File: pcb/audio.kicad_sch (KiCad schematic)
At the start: 0 parts

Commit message: WIP schematic
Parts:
- added C10, C8, C9: 0.1µF, symbol Device:C_Small
- added C5, C6, C7: 0.33µF, symbol Device:C_Small
- added D1, D2, D3: RED, symbol Device:LED_Small_Filled
- added HS1: OMNI-220-18-75-3C, symbol Mechanical:Heatsink_Pad_2Pin
- added Q1, Q2, Q3: BC547, Package_TO_SOT_THT:TO-92_Inline, symbol Transistor_BJT:BC547
- added R1, R3: 910Ω, symbol Device:R_Small
- added R10, R11, R12, R13, R14, R15, R16, R4, R5, R6, R7, R8, R9: R, symbol Device:R
- added R2: 390Ω, symbol Device:R_Small
- added TP1, TP2, TP3, TP4, TP5, TP6, TP7: TestPoint_Probe, symbol Connector:TestPoint_Probe
- added U52: LM7809_TO220, Package_TO_SOT_THT:TO-220-3_Vertical, symbol Regulator_Linear:LM7809_TO220
- added U53: LM7805_TO220, Package_TO_SOT_THT:TO-220-3_Vertical, symbol Regulator_Linear:LM7805_TO220
- added U54: LM7909_TO220, Package_TO_SOT_THT:TO-220-3_Vertical, symbol Regulator_Linear:LM7909_TO220
- added U55, U58: 4504, symbol 4xxx:4504
- added U56, U57, U59, U61: 4053, symbol 4xxx:4053
- added U60: TL072, symbol Amplifier_Operational:TL072
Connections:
- new net: R11.1, U61.14 (X)
- new net: R11.2, R12.2, R13.2, R14.2, R15.2, R16.1, U60.6 (-)
- new net: Q3.2 (B), R6.2
- new net: D2.2 (A), R2.2
- new net: Q2.2 (B), R5.2
- new net: Q1.2 (B), R4.2
- new net: D1.2 (A), R1.2
- new net: U58.12 (Eout), U59.10 (B)
- new net: U58.10 (Dout), U59.11 (A)
- new net: U59.12 (X0), U61.12 (X0)
- new net: R7.1, U59.14 (X)
- new net: R8.1, U59.15 (Y)
- new net: U59.2 (Y0), U61.2 (Y0)
- new net: R9.1, U59.4 (Z)
- new net: U57.2 (Y0), U59.5 (Z0), U61.5 (Z0)
- new net: U58.15 (Fout), U59.9 (C)
- new net: R10.1, R7.2, R8.2, R9.2, U60.2 (-)
- new net: U55.10 (Dout), U57.11 (A)
- new net: U55.12 (Eout), U57.10 (B)
- new net: U55.15 (Fout), U57.9 (C)
- new net: U55.2 (Aout), U56.11 (A)
- new net: U55.4 (Bout), U56.10 (B)
- new net: U55.6 (Cout), U56.9 (C)
- new net: U58.4 (Bout), U61.10 (B)
- new net: U58.2 (Aout), U61.11 (A)
- new net: R12.1, U61.15 (Y)
- new net: R13.1, U61.4 (Z)
- new net: U58.6 (Cout), U61.9 (C)
- new net: D3.1 (K), R3.2
- new net: R10.2, U60.1
- new net: R16.2, U60.7
- new net: U57.14 (X), U57.5 (Z0)
- new net +12V: C5.1, C6.1, TP1.1, TP2.1, U52.1 (VI), U53.1 (VI)
- new net +5VA: C9.1, R2.1, TP6.1, U53.3 (VO), U55.1 (VCC), U58.1 (VCC)
- new net +9VA: C8.1, R1.1, TP5.1, U52.3 (VO), U55.16 (VDD), U56.16 (VDD), U57.16 (VDD), U58.16 (VDD), U59.16 (VDD), U60.8 (V+), U61.16 (VDD)
- new net -12V: C7.1, TP3.1, U54.2 (VI)
- new net -9VA: C10.1, R3.1, TP7.1, U54.3 (VO), U56.7 (VEE), U57.7 (VEE), U59.7 (VEE), U60.4 (V-), U61.7 (VEE)
- new net DC3: U55.14 (Fin)
- new net FILTER0: U58.9 (Din)
- new net FILTER1: U58.11 (Ein)
- new net FILTER2: U58.14 (Fin)
- new net FM12: U55.11 (Ein)
- new net GNDA: C10.2, C5.2, C6.2, C7.2, C8.2, C9.2, D1.1 (K), D2.1 (K), D3.2 (A), HS1.1, HS1.2, Q1.3 (E), Q2.3 (E), Q3.3 (E), TP4.1, U52.2 (GND), U53.2 (GND), U54.1 (GND), U55.8 (VSS), U56.6 (Inh), U56.8 (VSS), U57.6 (Inh), U57.8 (VSS), U58.8 (VSS), U59.1 (Y1), U59.13 (X1), U59.3 (Z1), U59.6 (Inh), U59.8 (VSS), U60.3 (+), U60.5 (+), U61.1 (Y1), U61.13 (X1), U61.3 (Z1), U61.6 (Inh), U61.8 (VSS)
- new net MIX0: U58.3 (Ain)
- new net MIX1: U58.5 (Bin)
- new net MIX2: U58.7 (Cin)
- new net OCTAVE0: R4.1
- new net OCTAVE2: R5.1
- new net OCTAVE3: R6.1
- new net Voice 0/FM/OCTAVE: Q1.1 (C)
- new net Voice 0/SQUARE: U56.12 (X0)
- new net Voice 0/TRIANGLE: U56.13 (X1)
- new net Voice 1/FM/OCTAVE: U57.1 (Y1)
- new net Voice 1/SQUARE: U56.2 (Y0)
- new net Voice 1/TRIANGLE: U56.1 (Y1)
- new net Voice 2/FM/OCTAVE: Q2.1 (C)
- new net Voice 2/SQUARE: U56.5 (Z0)
- new net Voice 2/TRIANGLE: U56.3 (Z1)
- new net Voice 3/FM/OCTAVE: Q3.1 (C)
- new net Voice 3/SQUARE: U57.12 (X0)
- new net Voice 3/TRIANGLE: U57.13 (X1)
- new net WAVEFORM0: U55.3 (Ain)
- new net WAVEFORM1: U55.5 (Bin)
- new net WAVEFORM2: U55.7 (Cin)
- new net WAVEFORM3: U55.9 (Din)
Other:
- added sheet Filter (filter.kicad_sch)
- added sheet Volume 0 (volume.kicad_sch)
- added sheet Volume 1 (volume.kicad_sch)
- added sheet Volume 2 (volume.kicad_sch)
- added sheet Volume 3 (volume.kicad_sch)
- sheet Voice 0 ports: added FM/OCTAVE, PWM, SQUARE, TRIANGLE; removed none
- sheet Voice 1 ports: added FM/OCTAVE, PWM, SQUARE, TRIANGLE; removed none
- sheet Voice 2 ports: added FM/OCTAVE, PWM, SQUARE, TRIANGLE; removed none
- sheet Voice 3 ports: added FM/OCTAVE, PWM, SQUARE, TRIANGLE; removed none
- note added: "+5VA OK"
- note added: "+9VA OK"
- note added: "-9VA OK"
- note added: "Analog Power"

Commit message: WIP PCB
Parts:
- added Q?: BC547, Package_TO_SOT_THT:TO-92_Inline, symbol Transistor_BJT:BC547
- added R? (x2): 10kΩ, symbol Device:R
- added R?: R, symbol Device:R
- renumbered C9 to C?, C5 to C?, C7 to C?, C10 to C?, C6 to C?, C8 to C?, D2 to D?, D1 to D?, D3 to D?, HS1 to HS?, Q3 to Q?, Q1 to Q?, Q2 to Q?, R11 to R?, R5 to R?, R7 to R?, R4 to R?, R15 to R?, R9 to R?, R8 to R?, R12 to R?, R14 to R?, R16 to R?, R13 to R?, R2 to R?, R10 to R?, R1 to R?, R6 to R?, R3 to R?, TP3 to TP?, TP7 to TP?, TP6 to TP?, TP1 to TP?, TP4 to TP?, TP5 to TP?, TP2 to TP?, U52 to U?, U54 to U?, U59 to U?, U55 to U?, U60 to U?, U53 to U?, U61 to U?, U58 to U?, U56 to U?, U57 to U?
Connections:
- net -9VA: now also R?.2
- net GNDA: now also Q?.3 (E), R?.1
- net Voice 1/FM/OCTAVE: now also U?.15 (Y); no longer U?.1 (Y1)
- net Envelope/OUT0: now reaches U?.12 (X0), U?.12 (X0)
- net Envelope/OUT1: now reaches U?.2 (Y0), U?.2 (Y0)
- net Envelope/OUT2: now reaches U?.2 (Y0), U?.5 (Z0), U?.5 (Z0)
- net Envelope/OUT3: now reaches R?.1
- net Envelope/IN0: now reaches U?.14 (X)
- net Envelope/IN1: now reaches U?.15 (Y)
- net Envelope/IN2: now reaches U?.4 (Z)
- net at U?.3 (Z1): now also R?.1, R?.2
- net Envelope/IN3: now reaches U?.4 (Z)
- new net: Q?.2 (B), R?.2
- new net: Q?.1 (C), U?.1 (Y1)
- new net OCTAVE1: R?.1
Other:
- sheet Volume 0 renamed Envelope
- removed sheet Volume 1
- removed sheet Volume 2
- removed sheet Volume 3
- sheet Envelope ports: added D0, D1, D2, D3, D4, D5, D6, D7, IN0, IN1, IN2, IN3, LOAD0, LOAD1, LOAD2, LOAD3, OUT0, OUT1, OUT2, OUT3; removed none
- moved on the sheet: Q?, R?, U?, U?A, U?B

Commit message: WIP PCB
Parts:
- added R? (x2): 220kΩ, symbol Device:R
- added U? (x7): 74HC14, symbol 74xx:74HC14
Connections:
- net +5VA: now also U?.14 (VCC)
- net GNDA: now also U?.7 (GND)
- net PWM0: now also U?.1
- net PWM1: now also U?.3
- net PWM2: now also U?.5
- net PWM3: now also U?.9
- net Filter/OUT: now reaches R?.1
- net Filter/IN: now reaches R?.2, U?.1
- net at R?.2, U?.7: now also R?.1
- new net: R?.2, U?.12
- new net: R?.2, U?.13
- new net Filter/PWM: U?.10
- new net Filter/Z0: U?.11
- new net Filter/Z1: R?.1
- new net Voice 0/PWM: U?.2
- new net Voice 1/PWM: U?.4
- new net Voice 2/PWM: U?.6
- new net Voice 3/PWM: U?.8
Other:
- sheet Filter ports: added IN, OUT, PWM, RESON0, RESON1, SELECT, Z, Z0, Z1; removed none
- moved on the sheet: Q?, R?, U?, U?A, U?B

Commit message: wip schematic
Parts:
- removed U? (x7): 74HC14, symbol 74xx:74HC14
- added D? (x2): BAT46, Diode_THT:D_DO-35_SOD27_P7.62mm_Horizontal, symbol Diode:BAT46
- added U?: 74HC245, symbol 74xx:74HC245
- R?: value 220kΩ -> 470Ω
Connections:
- net +5VA: now also D?.1 (K), U?.1 (A->B), U?.20 (VCC)
- net GNDA: now also D?.2 (A), U?.10 (GND), U?.8 (A6), U?.9 (A7)
- net PWM0: now also U?.2 (A0)
- net PWM1: now also U?.3 (A1)
- net PWM2: now also U?.4 (A2)
- net PWM3: now also U?.5 (A3)
- net Voice 0/PWM: now also U?.18 (B0)
- net Voice 1/PWM: now also U?.17 (B1)
- net Voice 2/PWM: now also U?.16 (B2)
- net Voice 3/PWM: now also U?.15 (B3)
- net STB5: now reaches R?.2
- net STB5: now also U?.13 (B5)
- net STA5: now reaches R?.2
- net STA5: now also D?.1 (K), D?.2 (A), U?.7 (A5)
- new net FLOAT: U?.19 (CE)
- new net STA4: U?.6 (A4)
- new net STB4: U?.14 (B4)
- no-connect marks 0 -> 2
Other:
- note added: "IN"
- note added: "OUT"

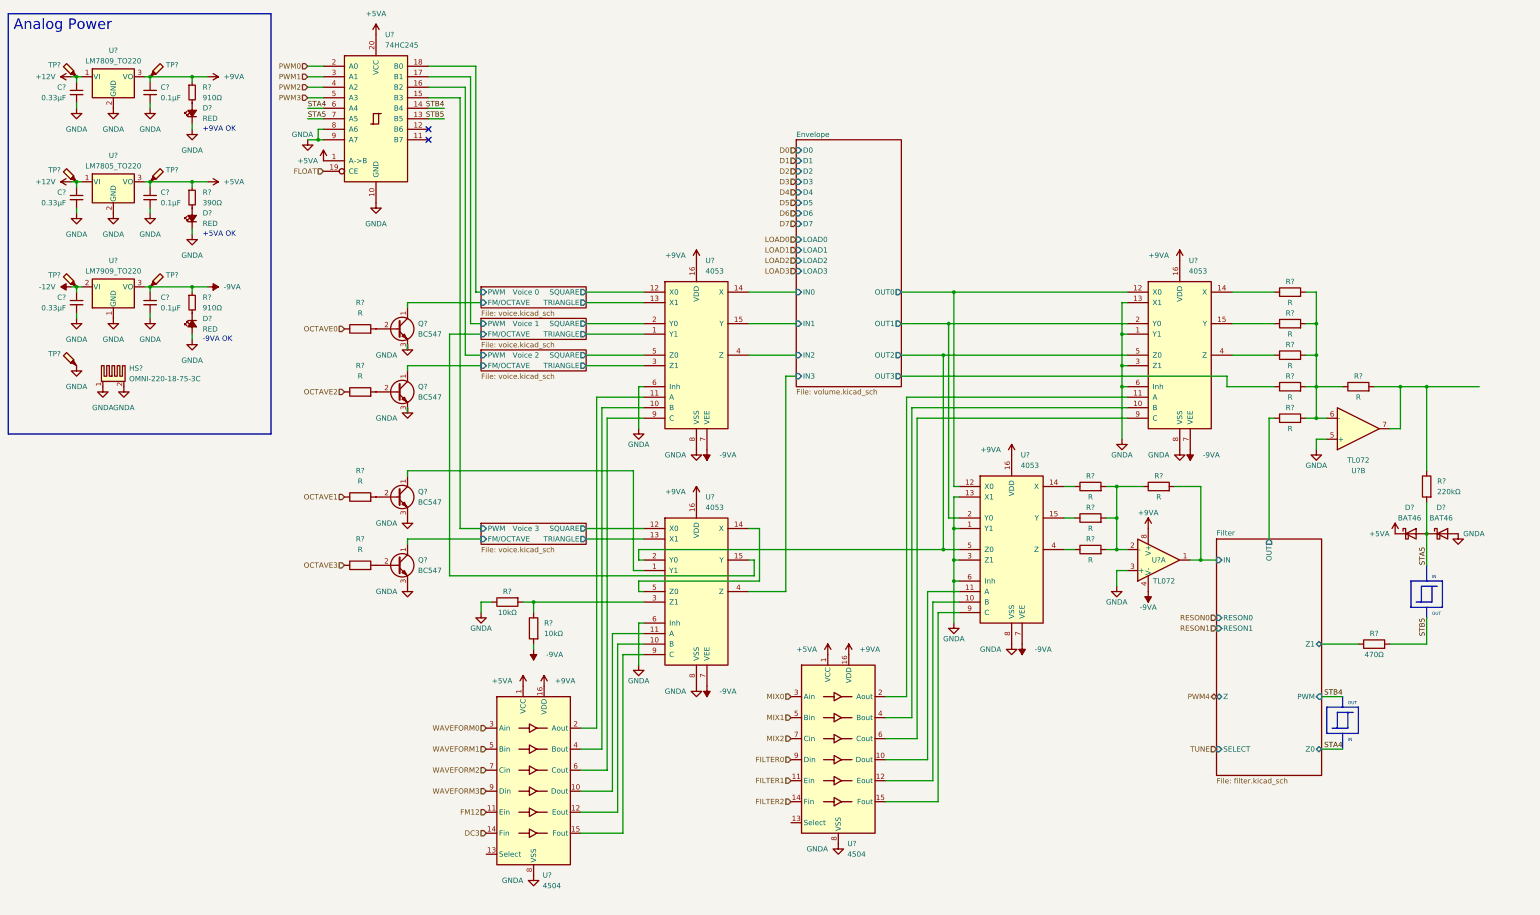
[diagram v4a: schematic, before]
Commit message: PCB: add reset circuit, xtal
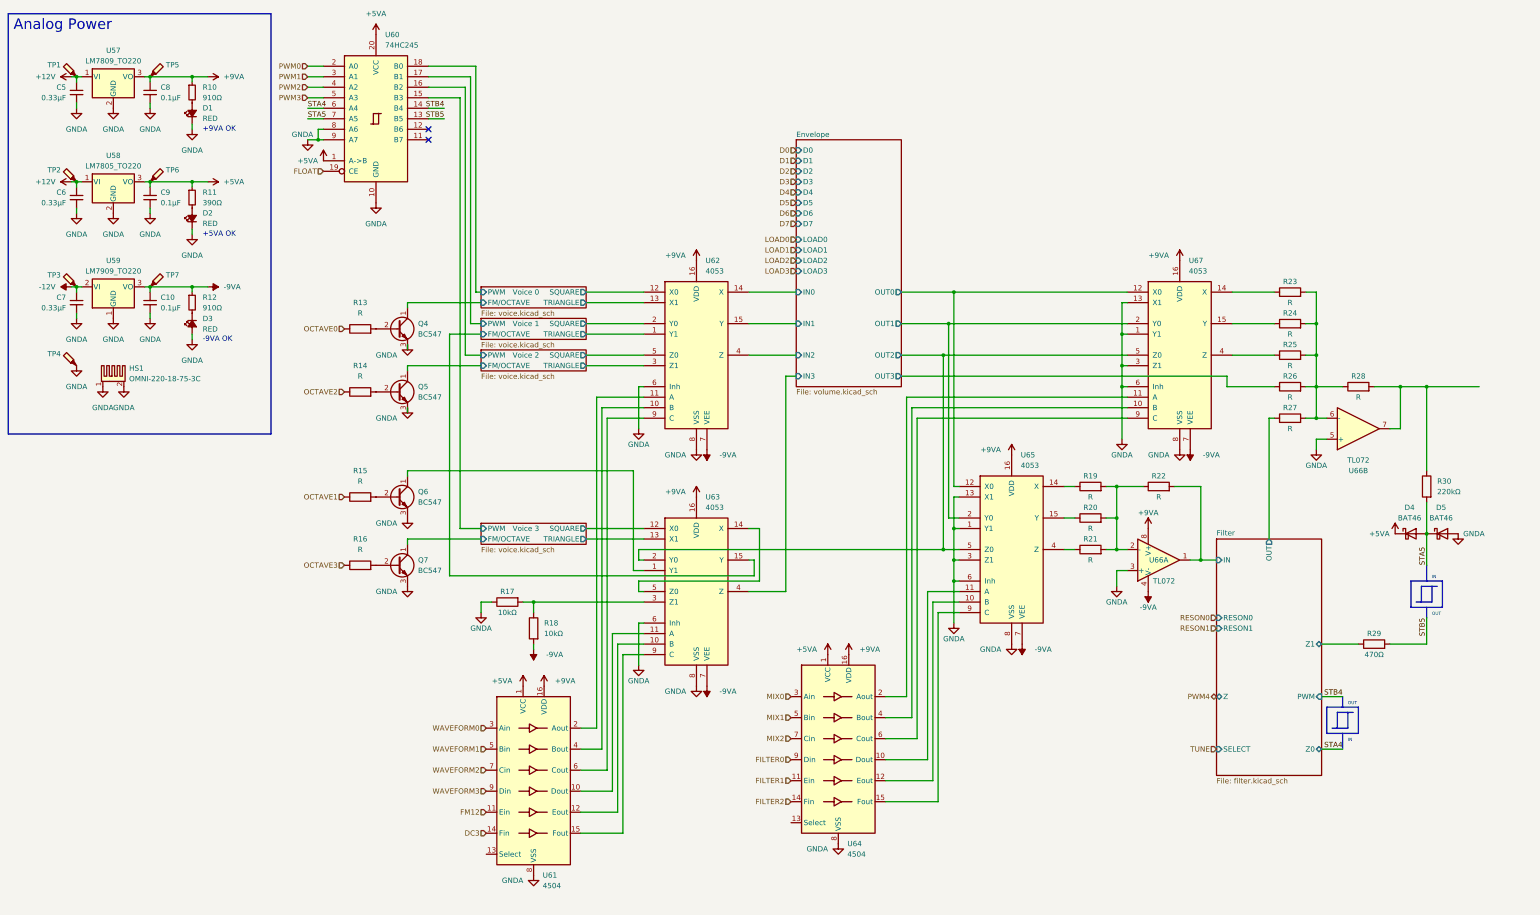
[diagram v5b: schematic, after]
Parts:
- gave numbers to parts that had none: 55

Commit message: WIP schematic
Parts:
- added NT1: NetTie_2, symbol Device:NetTie_2
- renumbered C6 to C10, C7 to C11, C8 to C12, C9 to C13, C10 to C14, C5 to C9, D1 to D2, D2 to D3, D3 to D4, D4 to D5, D5 to D6, Q7 to Q10, Q4 to Q7, Q5 to Q8, Q6 to Q9, R10 to R17, R11 to R18, R12 to R19, R13 to R20, R14 to R21, R15 to R22, R16 to R23, R17 to R24, R18 to R25, R19 to R26, R20 to R27, R21 to R28, R22 to R29, R23 to R30, R24 to R31, R25 to R32, R26 to R33, R27 to R34, R28 to R35, R29 to R36, R30 to R37, U57 to U58, U58 to U59, U59 to U60, U60 to U61, U61 to U62, U62 to U63, U63 to U64, U64 to U65, U65 to U66, U66 to U67, U67 to U68
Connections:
- net GNDA: now also U62.13 (Select), U65.13 (Select), NT1.2
- new net GND: NT1.1

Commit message: WIP schematic
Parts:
- added C18: 0.27µF, symbol Device:C
- added C19: 5pF, symbol Device:C_Small
- added D4, D5: 1N4148, symbol Device:D_Filled
- added J8: Headphones, symbol Connector_Audio:AudioJack3
- added Q11: BC338, Package_TO_SOT_THT:TO-92_Inline, symbol Transistor_BJT:BC338
- added Q12: BC328, Package_TO_SOT_THT:TO-92_Inline, symbol Transistor_BJT:BC328
- added R41, R46, R47: 10kΩ, symbol Device:R
- added R43: 56kΩ, symbol Device:R
- added R44: 330kΩ, symbol Device:R
- added R45: 22kΩ, symbol Device:R
- added R48, R49: 33kΩ, symbol Device:R
- added R53: 68Ω, symbol Device:R
- added RV1: 1kΩ, symbol Device:R_Potentiometer
- added TP1, TP9: TestPoint_Probe, symbol Connector:TestPoint_Probe
- added U66: TL074, symbol Amplifier_Operational:TL074
- renumbered C9 to C20, C10 to C21, C11 to C22, C12 to C23, C13 to C24, C14 to C25, D5 to D2, D6 to D3, D2 to D6, D3 to D7, D4 to D8, R20 to R24, R21 to R25, R22 to R26, R23 to R27, R24 to R28, R25 to R29, R26 to R30, R27 to R31, R28 to R32, R29 to R33, R30 to R34, R31 to R35, R32 to R36, R33 to R37, R34 to R38, R35 to R39, R36 to R40, R37 to R42, R17 to R50, R18 to R51, R19 to R52, TP1 to TP2, TP2 to TP3, TP3 to TP4, TP4 to TP5, TP5 to TP6, TP6 to TP7, TP7 to TP8, U61 to U58, U62 to U59, U63 to U60, U64 to U61, U65 to U62, U66 to U63, U67 to U64, U68 to U65, U58 to U67, U59 to U68, U60 to U69
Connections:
- net +9VA: now also Q11.1 (C), R46.1
- net -9VA: now also Q12.1 (C), R47.2
- net GNDA: now also J8.S, R45.2, RV1.1
- net at R39.2, R42.1, U64.7: now also R41.2, TP1.1
- new net: R43.1, RV1.2
- new net: R41.1, RV1.3
- new net: J8.R, J8.T, R53.2
- new net: C19.1, R44.1, R48.2, R49.1, R53.1, TP9.1, U66.8
- new net: C18.2, C19.2, R44.2, U66.9 (-)
- new net: Q11.3 (E), R48.1
- new net: D4.2 (A), Q11.2 (B), R46.2
- new net: D5.1 (K), Q12.2 (B), R47.1
- new net: D4.1 (K), D5.2 (A)
- new net: Q12.3 (E), R49.2
- new net: R45.1, U66.10 (+)
- new net: C18.1, R43.2
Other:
- moved on the sheet: C20, C21, C22, C23, C24, C25, D2, D3, D6, D7, D8, HS1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

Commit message: WIP schematic
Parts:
- renumbered C18 to C23, C19 to C24, C20 to C25, C21 to C26, C22 to C27, C23 to C28, C24 to C29, C25 to C30, J8 to J9
